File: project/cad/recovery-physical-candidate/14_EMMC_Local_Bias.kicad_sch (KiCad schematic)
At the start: 12 parts

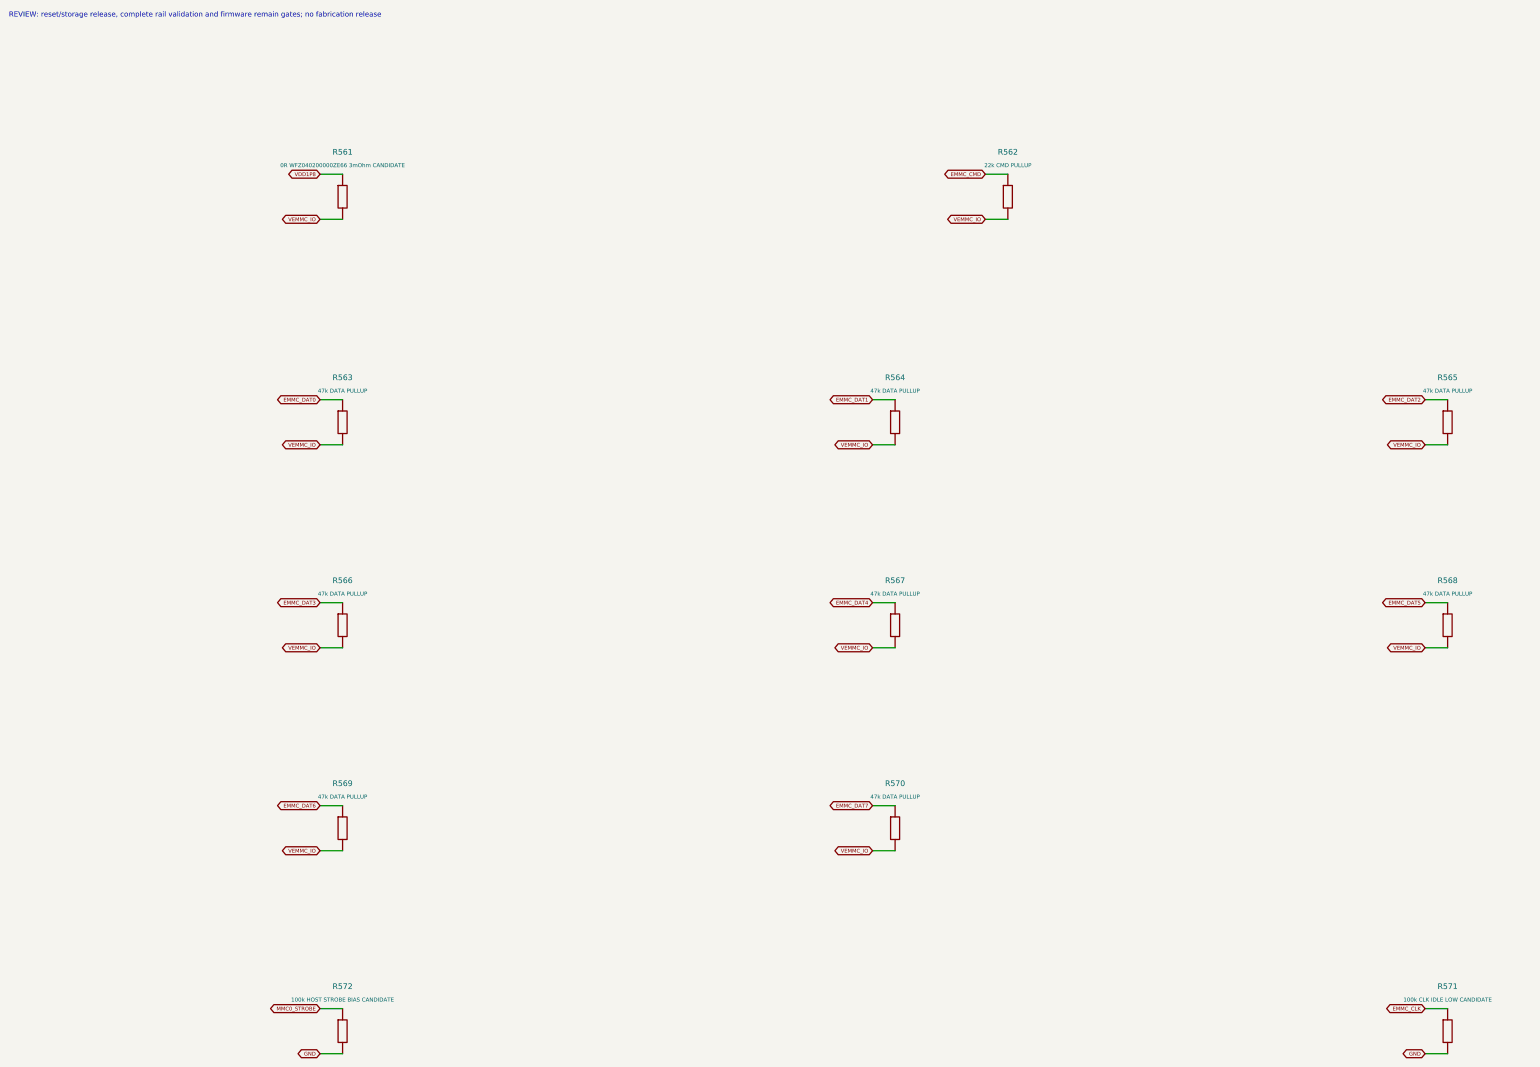
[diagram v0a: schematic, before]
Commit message: Add R5 conditional 43k eMMC DAT pullup checkpoint
Change only R563-R570 Value and Footprint fields to 43k CRCW020143K0FKED candidates. Preserve 254 references, 457 nets, 1509 pin/function/type/net bindings and all other exported component/population attributes. Coverage: 166 assigned, 88 gaps; R528 DNP preserved.
Fresh KiCad 9.0.2 export and ERC plus full-attribute independent comparison pass on the exact public copy. The required +/-10% total resistance envelope gives 38.7-47.3k within the cited 10-50k source range; this is not an arbitrary-life guarantee.
CORE PG material is review-only with an unchanged-graph bridge; no supervisor alternative or topology change adopted.
28 changed/new files only; retain root 哦READ.MD and prior history. Lifetime, leakage, SI, ROM, whole-board routing and manufacturing qualification remain open.
Source manifest SHA256: f823cfe471f18b033cac6a5e49e0779dbf70a6ecaa91d596b80d3d246bebc3a8
Delta ZIP SHA256: 831d57d6a82cdfff4a8233b36b96ac528480c84d9f9381d4fe095ebd97077f51
Verified tree: c1766fa4d77f6c610886ca83299bb7f9297e5fd4
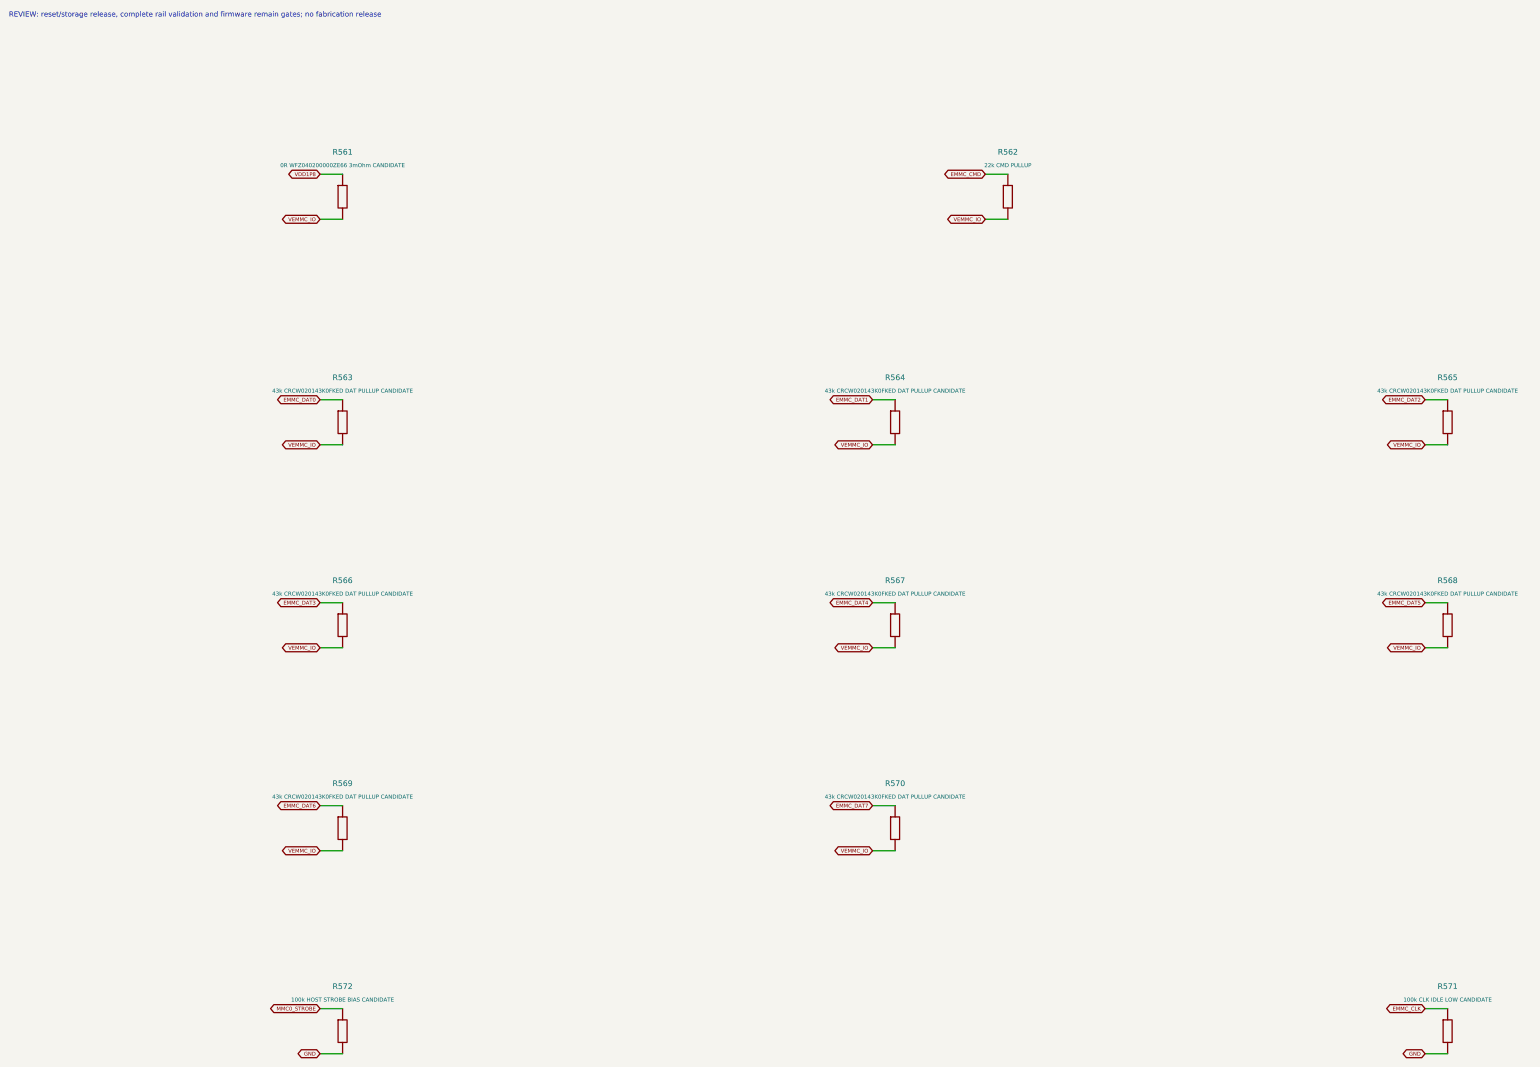
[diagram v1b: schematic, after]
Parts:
- R563, R564, R565, R566, R567, R568, R569, R570: value 47k DATA PULLUP -> 43k CRCW020143K0FKED DAT PULLUP CANDIDATE; footprint (none) -> CMK230_Recovery_Passive_Candidates:Vishay_CRCW0201_SourceLand_PROCESS_CANDIDATE

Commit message: Add R6 conditional passive footprint coverage
Assign candidates to 25 ordinary bias resistors and L21 only. Preserve all 254 component values, 457 nets, 1509 bindings and population attributes; R45/R47/R528 remain DNP. Coverage: 192 assigned, 62 gaps.
Exact publication-copy KiCad 9.0.2 export/ERC and full-component/graph comparison pass. L21 isolated six-layer fixture DRC passes; deliberate 1.40mm clearance rejects the 1.39mm gap. Native pad1 +X start mapping and recorded paste SVG aperture parity verified.
Keep independent graph, geometry and paste-override evidence. Three original explanatory/native-CAM SVGs inspected; no vendor pages, PDFs or runtime files uploaded.
60 changed/new files only; retain root 哦READ.MD and prior history. Not a complete core PCB or manufacturing, thermal, timing, switching-loop or DDR/PDN qualification.
Source manifest SHA256: 41e156fc71d4b10e1309578cfc231c354b290f847fc957d7bd48313e88f86145
Delta ZIP SHA256: 991fa45e6b49d84bdb60604ca1e232ea41bbe56994e89768a0dd62f8eb94a651
Verified tree: 4e28dc45a69ddc32ee629ba6cfef3bdfb46547ff
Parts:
- R562, R571, R572: footprint (none) -> CMK230_Recovery_Passive_Candidates:Vishay_CRCW0201_SourceLand_PROCESS_CANDIDATE

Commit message: R7: add conditional link footprints and fabricated copper features
Add ten footprint bindings and exclude JP1/TP81/TP82 from BOM; preserve all 254 values, 457 nets, 1509 pin/function/type/net bindings, on-board and DNP states. Coverage 202 assigned / 52 gaps.

Fresh KiCad 9.0.2 ERC passes. Independent exact-copy schematic, geometry, population, placement and CAM controls pass. Ten-reference isolated fixture has zero rule violations and three expected unrouted shared-net connections. Default paste still contains R528's two apertures despite DNP; explicit assembly/stencil variant remains a release gate. No complete core PCB, routing or manufacturing qualification.

Preserve 65 normalized source files plus manifest, source provenance, original CAD diagnostic SVG/CAM and root 哦READ.MD. Vendor originals excluded. All 1148 remote blobs verified against the local tree.

Manifest SHA256: 0fe14d3bf459b0f8046275165c57a58a2ab81769786d3e2496db5d605bf713fb
Delta ZIP SHA256: 3dfadf28c33240d59e85ee2e4374008a39fd3f1e564a0044020792ffa0f05c6e (230613 bytes)
Tree: c48cd1f548a5cd3a0ce28359b19fb4a988aab953
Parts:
- R561: footprint (none) -> CMK230_Recovery_Link_Candidates:Vishay_WFZ0402_SourceLand_PROCESS_CANDIDATE
